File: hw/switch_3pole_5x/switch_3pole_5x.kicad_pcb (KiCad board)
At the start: 2 copper layers, 93 x 67 mm, 101 parts, among them J1 WAGO 2081-1123, J10 tp_relay_1, J11 tp_relay_2, J12 CONN-ISP-6, J13 WAGO 243-723, J14 WAGO 243-724, J15 WAGO 243-721, J16 WAGO 243-722, J17 tp_relay_3, J18 tp_relay_4, J19 tp_button_0, J2 WAGO 2081-1123, J20 tp_button_1, J21 tp_button_2, J22 tp_button_3, J23 tp_button_4, J24 tp_cseep, J25 tp_miso, J26 tp_mosi, J27 tp_sck, J28 tp_txden, J29 tp_txd, J3 WAGO 2081-1123, J30 tp_rxd, J31 tp_vcc, J32 tp_gnd, J4 WAGO 2081-1123, J5 WAGO 2081-1123, J6 tp_relay_0, J7 WAGO 233-504, J8 WAGO 233-504, J9 WAGO 233-502, Q1 BSS138, Q2 BSS138, Q3 BSS138, Q4 BSS138, Q5 BSS138, U3 25LC256, U4 ATMEGA328-TQFP32, U5 7,3728MHz, U6 MAX487ECSA, U7 AM1S-2405

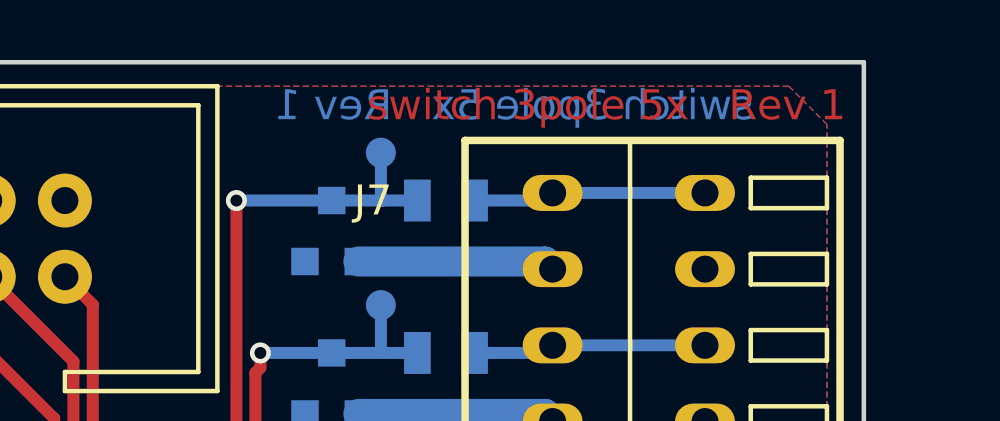
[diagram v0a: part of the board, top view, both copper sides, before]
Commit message: fixed switch_3pole_5x library references added component placement drawings updated 3d images and gerber files
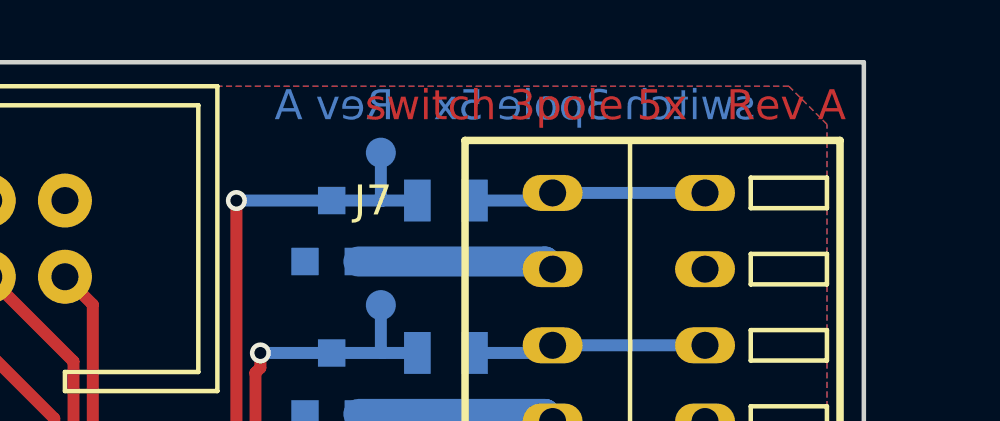
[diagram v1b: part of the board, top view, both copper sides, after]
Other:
- board text added: "switch 3pole 5x Rev A"
- board text removed: "switch 3pole 5x Rev 1"
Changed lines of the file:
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@@
     (title "motor switch 3pole 5x")
     (date 2018-09-19)
-    (rev 1)
+    (rev A)
     (company koewiba)
   )
   (layers
-    (0 F.Cu signal hide)
-    (31 B.Cu signal hide)
+    (0 F.Cu signal)
+    (31 B.Cu signal)
     (32 B.Adhes user)
     (33 F.Adhes user)
@@
       (drillshape 0)
       (scaleselection 1)
-      (outputdirectory "pcb/"))
+      (outputdirectory "gerber"))
   )
   (net 0 "")
@@
     (effects (font (size 1 1) (thickness 0.2)) (justify left))
   )
-  (gr_text "switch 3pole 5x   Rev 1" (at 173.355 51.435) (layer B.Cu)
+  (gr_text "switch 3pole 5x   Rev A" (at 173.355 51.435) (layer B.Cu)
     (effects (font (size 1 1) (thickness 0.2)) (justify right mirror))
   )
-  (gr_text "switch 3pole 5x   Rev 1" (at 192.405 51.435) (layer F.Cu)
+  (gr_text "switch 3pole 5x   Rev A" (at 192.405 51.435) (layer F.Cu)
     (effects (font (size 1 1) (thickness 0.2)) (justify right))
   )

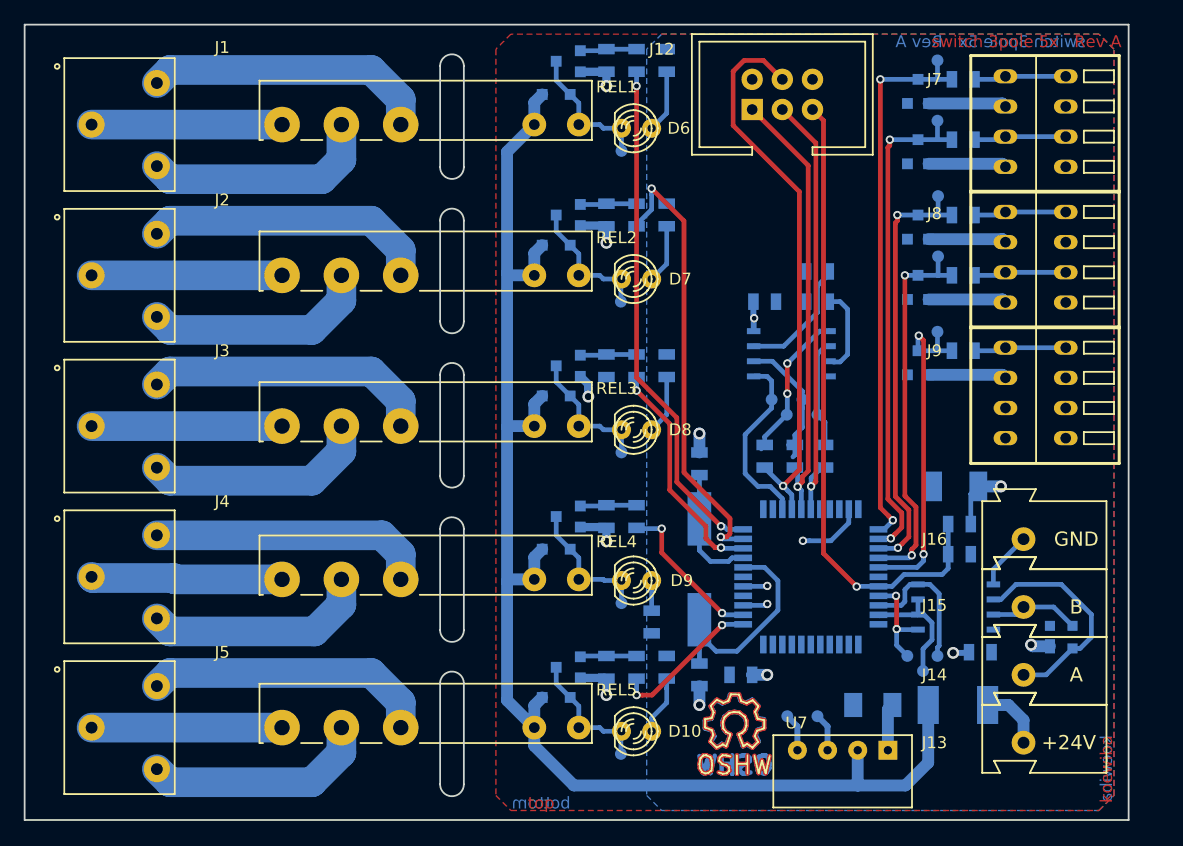
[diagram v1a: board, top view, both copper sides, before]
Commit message: Update to revision B. Fix footprint of U4 (TQFP32)
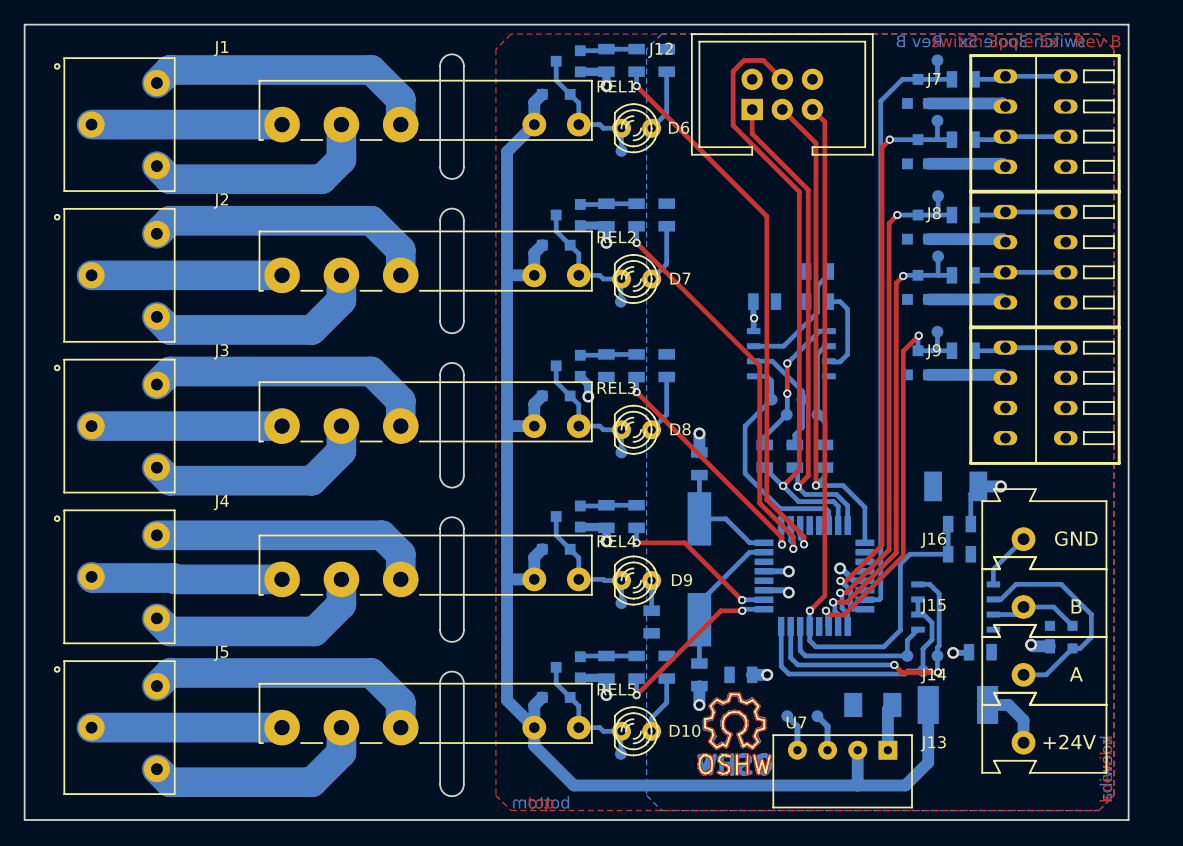
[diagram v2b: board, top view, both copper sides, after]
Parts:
- U4: footprint Housings_QFP:TQFP-44_10x10mm_Pitch0.8mm -> Housings_QFP:TQFP-32_7x7mm_Pitch0.8mm
- moved U4 0.31 mm to (166.5, 96.4)
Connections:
- D22 pad 2: (no net) -> Net-(D22-Pad2)
- R3 pad 2: (no net) -> Net-(R3-Pad2)
- U4 pad 12: (no net) -> /bus_atmega328_basic/PB0
- U4 pad 13: (no net) -> /bus_atmega328_basic/PB1
- U4 pad 19: (no net) -> /bus_atmega328_basic/ADC6
- U4 pad 20: (no net) -> /bus_atmega328_basic/AREF
- U4 pad 22: (no net) -> /bus_atmega328_basic/ADC7
- U4 pad 28: (no net) -> /bus_atmega328_basic/PC5
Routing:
- net /bus_atmega328_basic//RESET: track 53.8 -> 66.6 mm
- net /bus_atmega328_basic/TXD0: track 12.1 -> 24.4 mm, vias 0 -> 2
- net /bus_atmega328_basic/TXD0EN: track 10.6 -> 22.8 mm
- net //button_1: track 42.4 -> 50.0 mm
- net Net-(C5-Pad1): track 19.4 -> 12.3 mm
- net //button_2: track 36.8 -> 43.4 mm
- net //button_4: track 28.9 -> 35.0 mm
- net //button_3: track 32.6 -> 38.5 mm
- net /bus_atmega328_basic/PB5_SCK: track 37.0 -> 42.7 mm
- net /bus_atmega328_basic/RXD0: track 8.75 -> 13.8 mm, vias 2 -> 0
- net //button_0: track 46.7 -> 51.6 mm, vias 2 -> 0
- net /bus_atmega328_basic/PB3_MOSI: track 48.1 -> 52.8 mm
- net /bus_atmega328_basic//CSEEP: track 15.3 -> 20.0 mm
- net /bus_atmega328_basic/PB4_MISO: track 38.0 -> 42.5 mm
- net /relay_0: track 43.3 -> 47.4 mm
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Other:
- board text added: "switch 3pole 5x Rev B"
- board text removed: "switch 3pole 5x Rev A"
